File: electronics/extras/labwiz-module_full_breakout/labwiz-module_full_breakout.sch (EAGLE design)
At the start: 8 parts

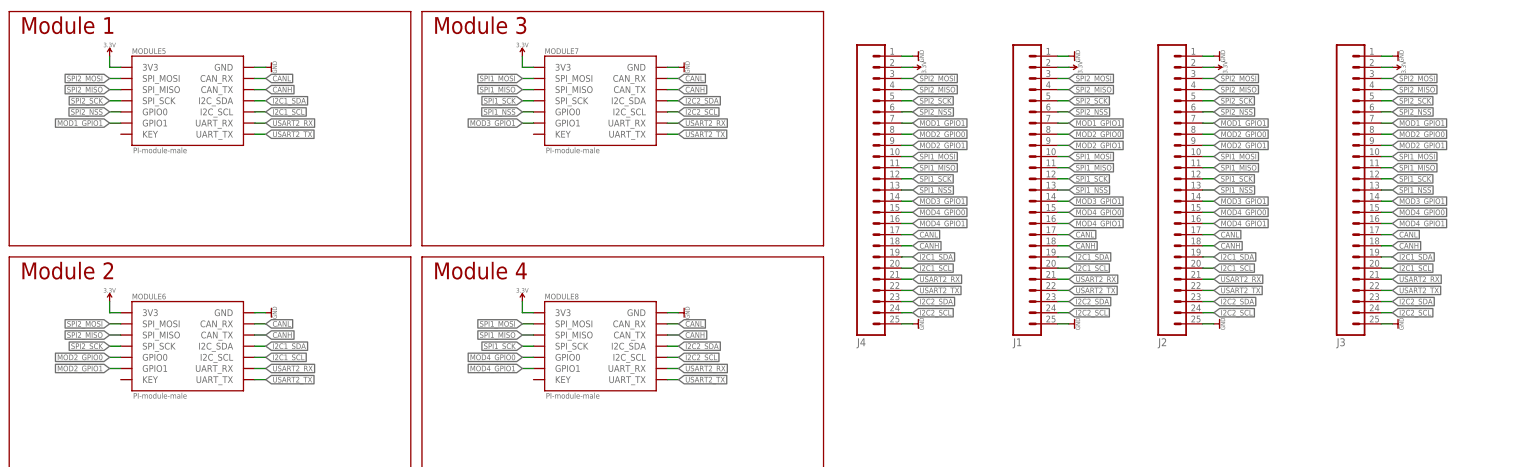
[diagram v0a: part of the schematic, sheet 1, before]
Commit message: Minor changes after design review. Will begin generating new gerbrs.
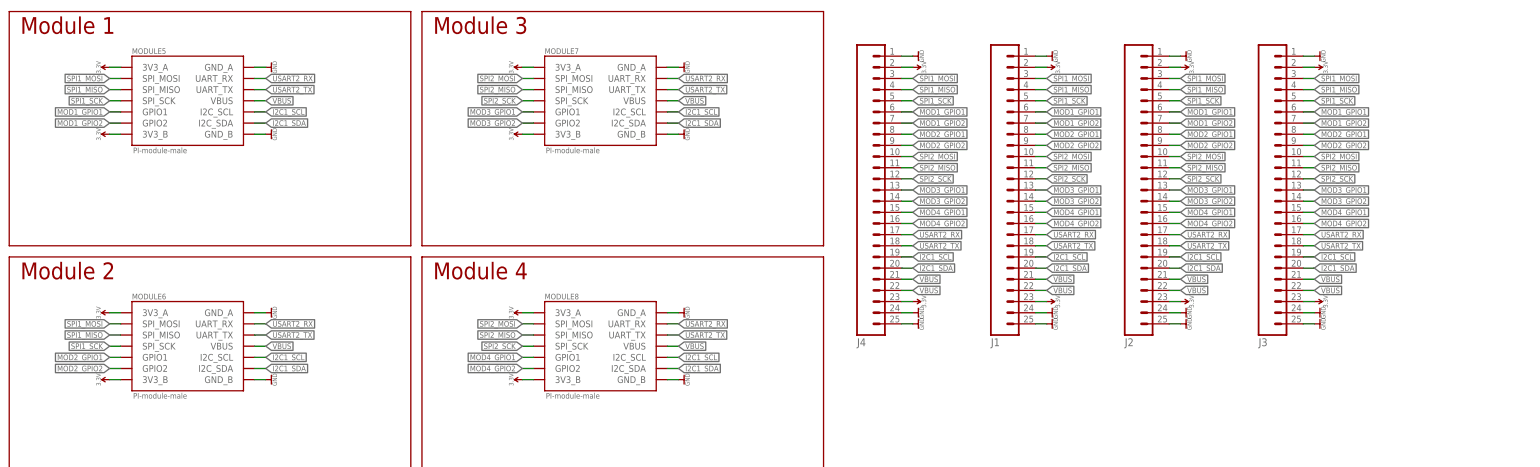
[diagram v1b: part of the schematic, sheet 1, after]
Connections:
- removed net CANH: J1.18, J2.18, J3.18, J4.18, MODULE5.CAN_TX, MODULE6.CAN_TX, MODULE7.CAN_TX, MODULE8.CAN_TX
- removed net CANL: J1.17, J2.17, J3.17, J4.17, MODULE5.CAN_RX, MODULE6.CAN_RX, MODULE7.CAN_RX, MODULE8.CAN_RX
- removed net I2C2_SCL: J1.24, J2.24, J3.24, J4.24, MODULE7.I2C_SCL, MODULE8.I2C_SCL
- removed net I2C2_SDA: J1.23, J2.23, J3.23, J4.23, MODULE7.I2C_SDA, MODULE8.I2C_SDA
- removed net MOD2_GPIO0: J1.8, J2.8, J3.8, J4.8, MODULE6.GPIO0
- removed net MOD4_GPIO0: J1.15, J2.15, J3.15, J4.15, MODULE8.GPIO0
- removed net SPI1_NSS: J1.13, J2.13, J3.13, J4.13, MODULE7.GPIO0
- removed net SPI2_NSS: J1.6, J2.6, J3.6, J4.6, MODULE5.GPIO0
- new net MOD1_GPIO2: J1.7, J2.7, J3.7, J4.7, MODULE5.GPIO2
- new net MOD2_GPIO2: J1.9, J2.9, J3.9, J4.9, MODULE6.GPIO2
- new net MOD3_GPIO2: J1.14, J2.14, J3.14, J4.14, MODULE7.GPIO2
- new net MOD4_GPIO2: J1.16, J2.16, J3.16, J4.16, MODULE8.GPIO2
- new net VBUS: J1.21, J1.22, J2.21, J2.22, J3.21, J3.22, J4.21, J4.22, MODULE5.VBUS, MODULE6.VBUS, MODULE7.VBUS, MODULE8.VBUS
- net 3.3V: now also J1.23, J2.23, J3.23, J4.23, MODULE5.3V3_A, MODULE5.3V3_B, MODULE6.3V3_A, MODULE6.3V3_B, MODULE7.3V3_A, MODULE7.3V3_B, MODULE8.3V3_A, MODULE8.3V3_B; no longer MODULE5.3V3, MODULE6.3V3, MODULE7.3V3, MODULE8.3V3
- net GND: now also J1.24, J2.24, J3.24, J4.24, MODULE5.GND_A, MODULE5.GND_B, MODULE6.GND_A, MODULE6.GND_B, MODULE7.GND_A, MODULE7.GND_B, MODULE8.GND_A, MODULE8.GND_B; no longer MODULE5.GND, MODULE6.GND, MODULE7.GND, MODULE8.GND
- net I2C1_SCL: now also J1.19, J2.19, J3.19, J4.19, MODULE7.I2C_SCL, MODULE8.I2C_SCL; no longer J1.20, J2.20, J3.20, J4.20
- net I2C1_SDA: now also J1.20, J2.20, J3.20, J4.20, MODULE7.I2C_SDA, MODULE8.I2C_SDA; no longer J1.19, J2.19, J3.19, J4.19
- net MOD1_GPIO1: now also J1.6, J2.6, J3.6, J4.6; no longer J1.7, J2.7, J3.7, J4.7
- net MOD2_GPIO1: now also J1.8, J2.8, J3.8, J4.8; no longer J1.9, J2.9, J3.9, J4.9
- net MOD3_GPIO1: now also J1.13, J2.13, J3.13, J4.13; no longer J1.14, J2.14, J3.14, J4.14
- net MOD4_GPIO1: now also J1.15, J2.15, J3.15, J4.15; no longer J1.16, J2.16, J3.16, J4.16
- net SPI1_MISO: now also J1.4, J2.4, J3.4, J4.4, MODULE5.SPI_MISO, MODULE6.SPI_MISO; no longer J1.11, J2.11, J3.11, J4.11, MODULE7.SPI_MISO, MODULE8.SPI_MISO
- net SPI1_MOSI: now also J1.3, J2.3, J3.3, J4.3, MODULE5.SPI_MOSI, MODULE6.SPI_MOSI; no longer J1.10, J2.10, J3.10, J4.10, MODULE7.SPI_MOSI, MODULE8.SPI_MOSI
- net SPI1_SCK: now also J1.5, J2.5, J3.5, J4.5, MODULE5.SPI_SCK, MODULE6.SPI_SCK; no longer J1.12, J2.12, J3.12, J4.12, MODULE7.SPI_SCK, MODULE8.SPI_SCK
- net SPI2_MISO: now also J1.11, J2.11, J3.11, J4.11, MODULE7.SPI_MISO, MODULE8.SPI_MISO; no longer J1.4, J2.4, J3.4, J4.4, MODULE5.SPI_MISO, MODULE6.SPI_MISO
- net SPI2_MOSI: now also J1.10, J2.10, J3.10, J4.10, MODULE7.SPI_MOSI, MODULE8.SPI_MOSI; no longer J1.3, J2.3, J3.3, J4.3, MODULE5.SPI_MOSI, MODULE6.SPI_MOSI
- net SPI2_SCK: now also J1.12, J2.12, J3.12, J4.12, MODULE7.SPI_SCK, MODULE8.SPI_SCK; no longer J1.5, J2.5, J3.5, J4.5, MODULE5.SPI_SCK, MODULE6.SPI_SCK
- net USART2_RX: now also J1.17, J2.17, J3.17, J4.17; no longer J1.21, J2.21, J3.21, J4.21
- net USART2_TX: now also J1.18, J2.18, J3.18, J4.18; no longer J1.22, J2.22, J3.22, J4.22
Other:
- moved on the sheet: J1, J2, J3
